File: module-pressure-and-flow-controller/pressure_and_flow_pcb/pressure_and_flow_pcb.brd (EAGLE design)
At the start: 36 x 19 mm, 38 parts, among them IC2 DSPIC33CK256MP502-I_SS, IC3 AD5624R, IC4 ADS1115, IC5 PCA9544APW,112, IC6 25AA040ST, X1 53047-04, X2 53047-04, X3 53047-04, X4 53047-04, X5 53047-04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

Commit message: Added bulk cap and changed caps to Kemet, which have smaller keepout.
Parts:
- added C10: (no value), rcl:C0603K
- C1, C2, C3, C4, C5, C6, C7, C8, C9: device rcl:C0603 -> rcl:C0603K
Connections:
- removed net N$33: IC2.22
- removed net N$37: IC2.28
- net +3V3: now also C10.1
- net GND: now also C10.2
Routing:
- net GND: track 46.3 -> 45.1 mm
- net +3V3: track 69.2 -> 70.2 mm, vias 5 -> 6
- net SPI2_MOSI: track 24.5 -> 25.1 mm

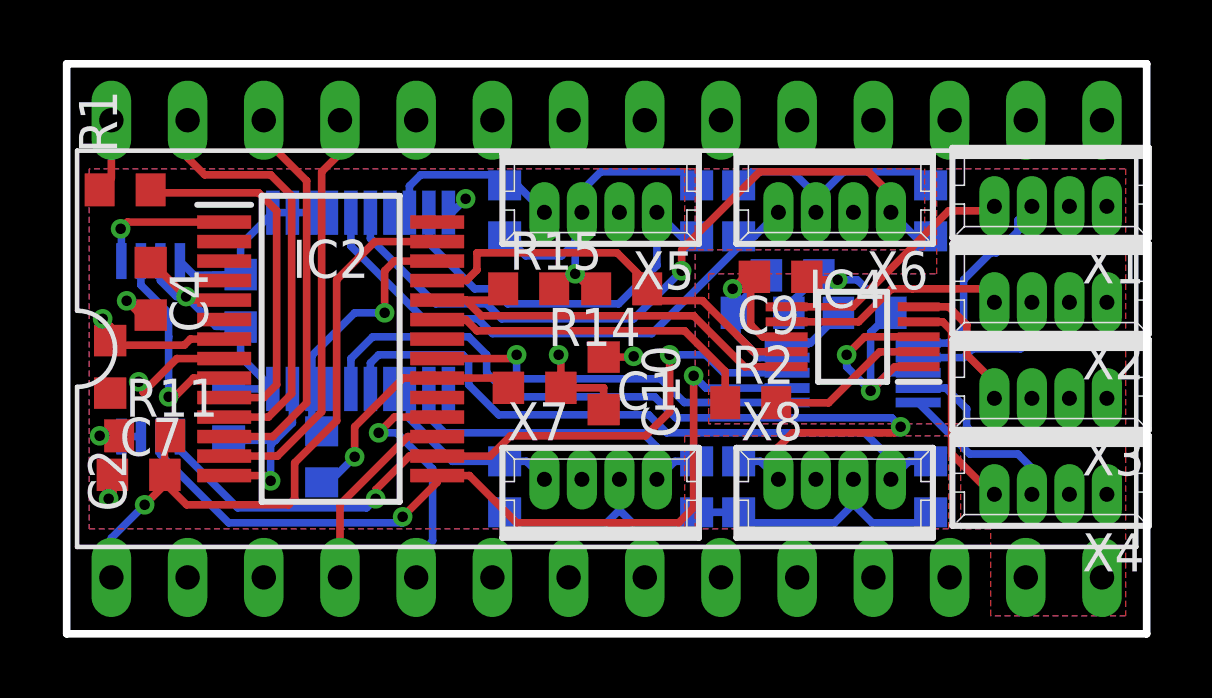
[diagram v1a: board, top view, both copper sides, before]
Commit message: PCB modifications to get I2C on correct pins and use extra SPI for EEPROM.  Code updated to match new pinout.
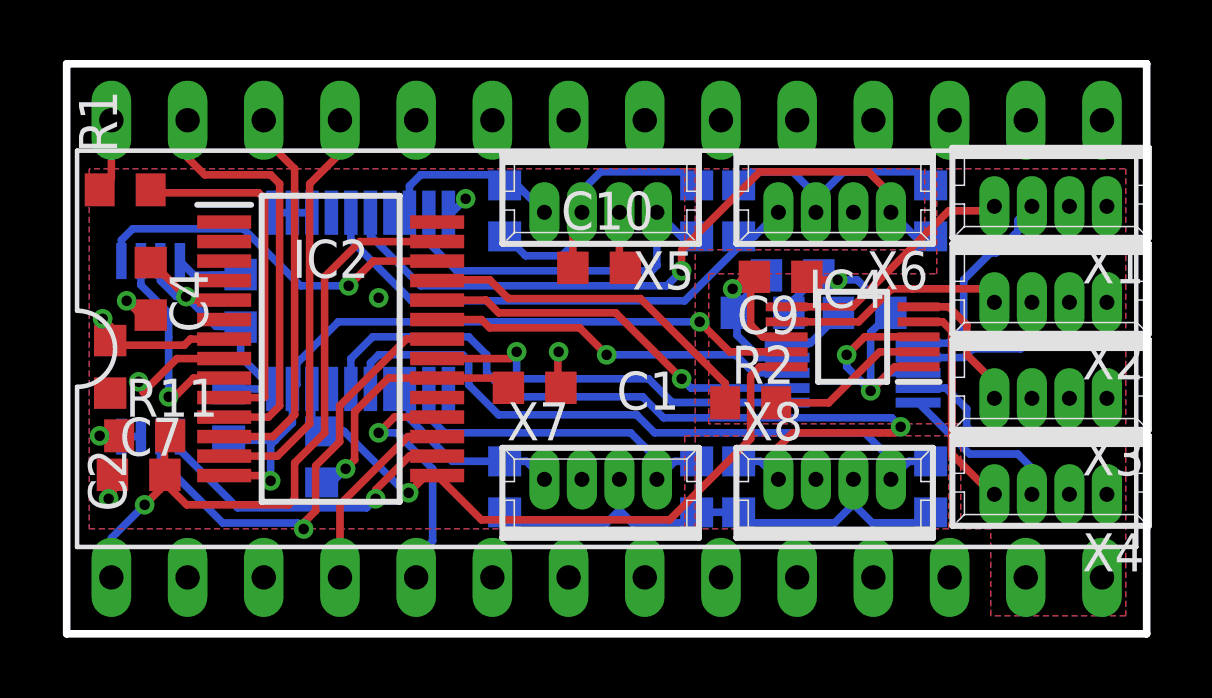
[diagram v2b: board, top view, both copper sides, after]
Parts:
- removed R14, R15: (no value), rcl:R0603
- moved C10 3.85 mm to (18.8, 12.7), turned to 0 degrees
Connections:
- net SPI2_MISO renamed SPI3_EE_MISO
- removed net ADC_SCL: IC2.24, IC4.10, R15.1
- removed net ADC_SDA: IC2.25, IC4.9, R14.1
- removed net SPI2_CLK: IC2.15, IC3.7, IC6.6
- removed net SPI2_EE_SS: IC2.1, IC6.1
- removed net SPI2_MOSI: IC2.16, IC3.8, IC6.5
- new net SPI2_DAC_CLK: IC2.24, IC3.7
- new net SPI2_DAC_MOSI: IC2.23, IC3.8
- new net SPI3_EE_CLK: IC2.22, IC6.6
- new net SPI3_EE_MOSI: IC2.16, IC6.5
- new net SPI3_EE_SS: IC2.26, IC6.1
- net +3V3: no longer R14.2, R15.2
- net ADC_RDY: now also IC2.25; no longer IC2.23
- net I2C_SCL: now also IC2.15, IC4.10; no longer IC2.26
- net I2C_SDA: now also IC4.9
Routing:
- net SPI2_CLK: track 28.8 -> 0.00 mm, vias 2 -> 0
- net SPI2_MOSI: track 25.1 -> 0.00 mm, vias 2 -> 0
- net I2C_SDA: track 6.53 -> 24.8 mm, vias 1 -> 2
- net SPI3_EE_CLK: track 0.00 -> 15.3 mm, vias 0 -> 1
- net ADC_SCL: track 14.9 -> 0.00 mm
- net ADC_SDA: track 14.0 -> 0.00 mm
- net I2C_SCL: track 8.96 -> 22.1 mm
- net SPI2_DAC_CLK: track 0.00 -> 12.9 mm, vias 0 -> 1
- net SPI3_EE_SS: track 0.00 -> 12.5 mm, vias 0 -> 1
- net SPI2_DAC_MOSI: track 0.00 -> 12.4 mm, vias 0 -> 1
- net SPI3_EE_MOSI: track 0.00 -> 10.7 mm, vias 0 -> 1
- net SPI2_EE_SS: track 4.63 -> 0.00 mm, vias 1 -> 0
- net GND: track 45.1 -> 42.3 mm, vias 8 -> 9
- net +3V3: track 70.2 -> 67.6 mm, vias 6 -> 4
- net N$14: track 18.5 -> 17.4 mm
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
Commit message: Pull up I2C MUX int pins to VCC.
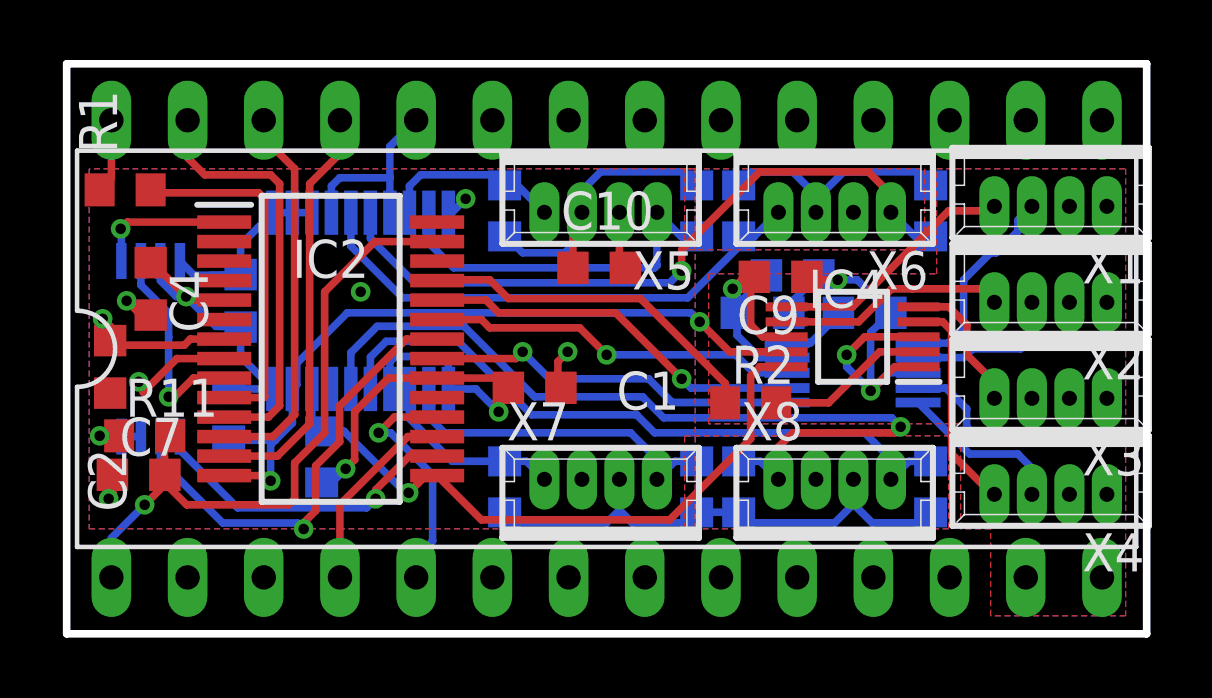
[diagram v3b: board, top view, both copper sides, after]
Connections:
- net +3V3: now also IC5.11, IC5.14, IC5.4, IC5.7
- net SPI3_EE_SS: now also IC2.1; no longer IC2.26
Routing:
- net +3V3: track 67.6 -> 79.8 mm, vias 4 -> 5
- net SPI3_EE_SS: track 12.5 -> 4.63 mm
- net GND: track 42.3 -> 44.9 mm
- net SPI2_DAC_SYNC: track 13.0 -> 12.5 mm

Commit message: More allowance between ICs and caps.
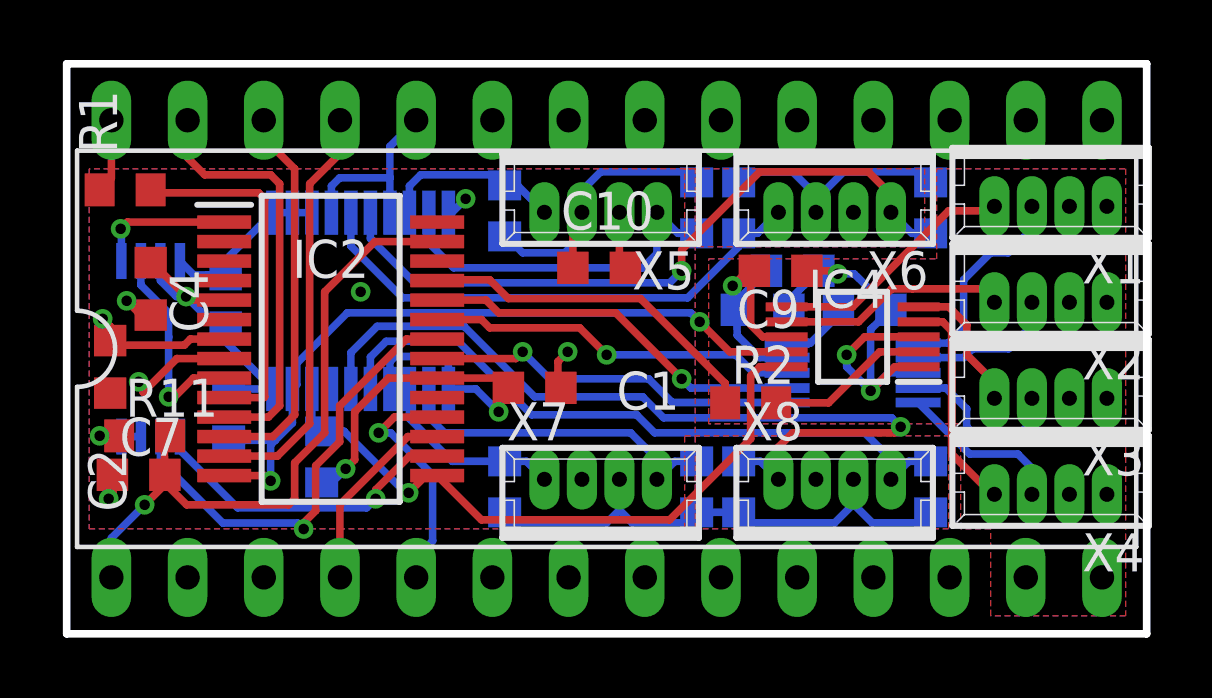
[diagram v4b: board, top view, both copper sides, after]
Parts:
- moved C8 0.50 mm to (6.30, 11.6)
- moved C9 0.20 mm to (24.8, 12.6)
- moved C6 0.15 mm to (25.2, 12.6)
- moved C3 0.10 mm to (27.6, 11.3)
- moved C5 0.10 mm to (24.2, 11.3)
- moved R4 0.10 mm to (22.0, 14.7)
- moved R5 0.10 mm to (23.4, 14.7)
- moved R6 0.10 mm to (29.8, 14.7)

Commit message: Caps moved to allow larger gaps near ADC, DAC, connector.
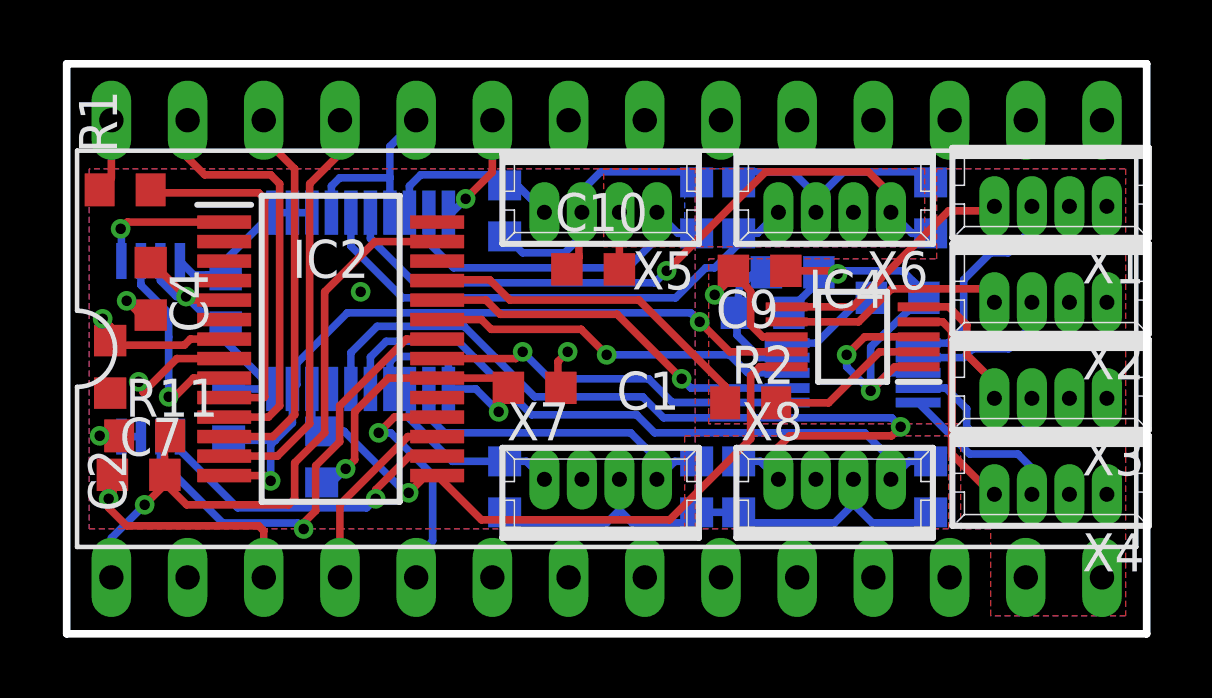
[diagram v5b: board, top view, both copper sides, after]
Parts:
- moved C3 1.17 mm to (28.7, 11.7)
- moved C9 0.70 mm to (24.1, 12.6)
- moved C10 0.21 mm to (18.6, 12.7)
- moved C5 0.10 mm to (24.2, 11.2)
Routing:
- net GND: track 44.8 -> 57.9 mm
- net N$1: track 2.31 -> 3.51 mm
- net +5V: track 22.6 -> 23.5 mm

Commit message: Component values added.
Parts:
- C1, C2, C3, C4, C5, C8, C9: value (none) -> 100nf
- C10, C6: value (none) -> 10uf
- R1, R10, R12, R13, R2, R3, R4, R5, R6, R7, R8, R9: value (none) -> 1k
- R11: value (none) -> 10k

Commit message: PCB documentation and images.
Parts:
- C6: value 10uf -> 10uf tantalum
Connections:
- net N$16 renamed I2C_DATA
- net N$17 renamed I2C_CLK
- net N$24 renamed PRESSURE_IN
- net N$3 renamed PRESSURE_OUT
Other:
- board text added: "12V"
- board text added: "12V GND"
- board text added: "3V3"
- board text added: "5V"
- board text added: "CLK"
- board text added: "Flow 1"
- board text added: "Flow 2"
- board text added: "Flow 3"
- board text added: "Flow 4"
- board text added: "GND"
- board text added: "ICSP PGC"
- board text added: "ICSP PGD"
- board text added: "MCLR"
- board text added: "MISO"
- board text added: "MOSI"
- board text added: "Pressure 1"
- board text added: "Pressure 2"
- board text added: "Pressure 3"
- board text added: "Pressure 4"
- board text added: "SS"
